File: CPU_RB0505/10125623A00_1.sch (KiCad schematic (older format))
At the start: 65 parts, among them IC3 K6R4016C1D-TI10, IC4 ST10F276, IC40 CD74HCT245M, IC41 74HCT1G04GW, IC42 74HCT1G32GW, IC43 74HCT1G32GW, IC44 NC7SZ66, Q1 8MHz, T6 2N7002

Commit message: ran renameSchSyms.py
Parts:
- C1, C3: symbol Flipped_Devices:C_Small -> Capacitor:C0603_22pF_50V_5%
- C10, C110, C116, C120, C22, C23, C25, C26, C27, C28, C29, C36, C51, C9: symbol Flipped_Devices:C_Small -> Capacitor:C0402_100nF_16V_10%
- C112, C114: symbol Flipped_Devices:C_Small -> Capacitor:C0805_1uF_16V_10%
- C14: symbol cpu-board:RES_4CB -> Capacitor:RES_4CB
- C6: symbol Flipped_Devices:C_Small -> Capacitor:C0805_330nF_16V_10%
- C7, C8: symbol Flipped_Devices:CP_Small -> Capacitor:C_1uF_35V_10%
- D10, D9: symbol Flipped_Devices:D_Schottky_A1K3 -> Diode:D_Schottky_A1K3_10022652
- D8: symbol Flipped_Devices:D_Zener_A1K3 -> Diode:D_Zener_A1K3_10022655
- Q1: symbol Device:Crystal_Small -> Crystal:Crystal_Small_10020993
- R1: symbol Flipped_Devices:R -> Resistor:R_100R_5%
- R10: symbol Flipped_Devices:R -> Resistor:R0603_1k5_5%
- R14: symbol Flipped_Devices:R -> Resistor:R0603_56k_1%
- R15: symbol Flipped_Devices:R -> Resistor:R0603_10k5_0.1%
- R3: symbol Flipped_Devices:R -> Resistor:R0603_220k_5%
- R46: symbol Flipped_Devices:R -> Resistor:R0603_22k_1%_10095983
- R60, R61: symbol Flipped_Devices:R -> Resistor:R_100k_5%
- R62: symbol Flipped_Devices:R -> Resistor:R0603_10k_5%
- R72: symbol Flipped_Devices:R -> Resistor:R_4k7_5%
- T6: symbol Flipped_Devices:Q_NMOS_GSD -> Transistor:Q_NMOS_GSD_10097274
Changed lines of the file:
@@
 $EndComp
 $Comp
-L Flipped_Devices:C_Small C?
+L Capacitor:C0402_100nF_16V_10% C?
 U 1 1 CB1F8FE5
 P 14700 2150
@@
 $EndComp
 $Comp
-L Flipped_Devices:C_Small C?
+L Capacitor:C0402_100nF_16V_10% C?
 U 1 1 A05C1986
 P 7350 9650
@@
 $EndComp
 $Comp
-L Flipped_Devices:C_Small C?
+L Capacitor:C0402_100nF_16V_10% C?
 U 1 1 93AA069D
 P 7350 9800
@@
 $EndComp
 $Comp
-L Flipped_Devices:C_Small C?
+L Capacitor:C0402_100nF_16V_10% C?
 U 1 1 5F5D481B
 P 7350 9950
@@
 $EndComp
 $Comp
-L Flipped_Devices:C_Small C?
+L Capacitor:C0402_100nF_16V_10% C?
 U 1 1 0EABB629
 P 7350 10100
@@
 $EndComp
 $Comp
-L Flipped_Devices:C_Small C?
+L Capacitor:C0402_100nF_16V_10% C?
 U 1 1 C9504634
 P 7350 10250
@@
 $EndComp
 $Comp
-L Flipped_Devices:C_Small C?
+L Capacitor:C0402_100nF_16V_10% C?
 U 1 1 AB97CB13
 P 7350 10400
@@
 $EndComp
 $Comp
-L Flipped_Devices:C_Small C?
+L Capacitor:C0402_100nF_16V_10% C?
 U 1 1 BCAFF6B0
 P 7350 10550
@@
 $EndComp
 $Comp
-L Flipped_Devices:C_Small C?
+L Capacitor:C0402_100nF_16V_10% C?
 U 1 1 284AD347
 P 7350 10700
@@
 $EndComp
 $Comp
-L Device:Crystal_Small Q?
+L Crystal:Crystal_Small_10020993 Q?
 U 1 1 F8782F37
 P 5650 1150
@@
 $EndComp
 $Comp
-L Flipped_Devices:R R?
+L Resistor:R_100R_5% R?
 U 1 1 E6C7F8B8
 P 5550 1350
@@
 $EndComp
 $Comp
-L Flipped_Devices:C_Small C?
+L Capacitor:C0805_330nF_16V_10% C?
 U 1 1 967579EA
 P 6550 1300
@@
 $EndComp
 $Comp
-L Flipped_Devices:CP_Small C?
+L Capacitor:C_1uF_35V_10% C?
 U 1 1 6D37B6AD
 P 7400 1100
@@
 $EndComp
 $Comp
-L Flipped_Devices:C_Small C?
+L Capacitor:C0402_100nF_16V_10% C?
 U 1 1 501DA122
 P 8450 1300
@@
 $EndComp
 $Comp
-L Flipped_Devices:C_Small C?
+L Capacitor:C0603_22pF_50V_5% C?
 U 1 1 7EE2FFE3
 P 5750 1050
@@
 $EndComp
 $Comp
-L Flipped_Devices:C_Small C?
+L Capacitor:C0603_22pF_50V_5% C?
 U 1 1 5ADCC44B
 P 5550 1050
@@
 $EndComp
 $Comp
-L Flipped_Devices:R R?
+L Resistor:R0603_56k_1% R?
 U 1 1 C54AB7D0
 P 2200 9550
@@
 $EndComp
 $Comp
-L Flipped_Devices:R R?
+L Resistor:R0603_10k5_0.1% R?
 U 1 1 BAB36D42
 P 2200 9850
@@
 $EndComp
 $Comp
-L Flipped_Devices:C_Small C?
+L Capacitor:C0402_100nF_16V_10% C?
 U 1 1 597E8BEF
 P 2200 10050
@@
 $EndComp
 $Comp
-L Flipped_Devices:R R?
+L Resistor:R0603_1k5_5% R?
 U 1 1 D628991E
 P 3100 5950
@@
 $EndComp
 $Comp
-L cpu-board:RES_4CB C?
+L Capacitor:RES_4CB C?
 U 1 1 8BD8962D
 P 2150 3950
@@
 $EndComp
 $Comp
-L Flipped_Devices:C_Small C?
+L Capacitor:C0402_100nF_16V_10% C?
 U 1 1 662809D9
 P 11150 1200
@@
 $EndComp
 $Comp
-L Flipped_Devices:D_Zener_A1K3 D?
+L Diode:D_Zener_A1K3_10022655 D?
 U 1 1 8A392F19
 P 12400 4250
@@
 $EndComp
 $Comp
-L Flipped_Devices:R R?
+L Resistor:R_4k7_5% R?
 U 1 1 CEF2471C
 P 12650 4050
@@
 $EndComp
 $Comp
-L Flipped_Devices:R R?
+L Resistor:R_100k_5% R?
 U 1 1 CCBE402C
 P 12050 7250
@@
 $EndComp
 $Comp
-L Flipped_Devices:C_Small C?
+L Capacitor:C0805_1uF_16V_10% C?
 U 1 1 9A495DAC
 P 12200 7250
@@
 $EndComp
 $Comp
-L Flipped_Devices:D_Schottky_A1K3 D?
+L Diode:D_Schottky_A1K3_10022652 D?
 U 1 1 59396773
 P 13950 7700
@@
 $EndComp
 $Comp
-L Flipped_Devices:R R?
+L Resistor:R0603_10k_5% R?
 U 1 1 F7CB6097
 P 4800 10950
@@
 $EndComp
 $Comp
-L Flipped_Devices:C_Small C?
+L Capacitor:C0402_100nF_16V_10% C?
 U 1 1 7614D321
 P 4800 10550
@@
 $EndComp
 $Comp
-L Flipped_Devices:C_Small C?
+L Capacitor:C0402_100nF_16V_10% C?
 U 1 1 150190AD
 P 10200 3250
@@
 	7950 1500 7950 1100
 $Comp
-L Flipped_Devices:CP_Small C?
+L Capacitor:C_1uF_35V_10% C?
 U 1 1 6F4029DE
 P 8250 1300
@@
 	12200 7700 12050 7700
 $Comp
-L Flipped_Devices:Q_NMOS_GSD T?
+L Transistor:Q_NMOS_GSD_10097274 T?
 U 1 1 78F4DB2D
 P 11850 6700
@@
 $EndComp
 $Comp
-L Flipped_Devices:R R?
+L Resistor:R0603_22k_1%_10095983 R?
 U 1 1 CBBF32AF
 P 12450 6700
@@
 Connection ~ 12050 6700
 $Comp
-L Flipped_Devices:D_Schottky_A1K3 D?
+L Diode:D_Schottky_A1K3_10022652 D?
 U 1 1 13A4EF58
 P 12450 6400
@@
 	14900 6850 14900 6800
 $Comp
-L Flipped_Devices:C_Small C?
+L Capacitor:C0805_1uF_16V_10% C?
 U 1 1 C17297D4
 P 14150 7300
@@
 Connection ~ 13650 7300
 $Comp
-L Flipped_Devices:R R?
+L Resistor:R_100k_5% R?
 U 1 1 CC254D70
 P 13800 7700
@@
 	5950 1550 5950 1600
 $Comp
-L Flipped_Devices:R R?
+L Resistor:R0603_220k_5% R?
 U 1 1 E7C109B0
 P 7150 1200

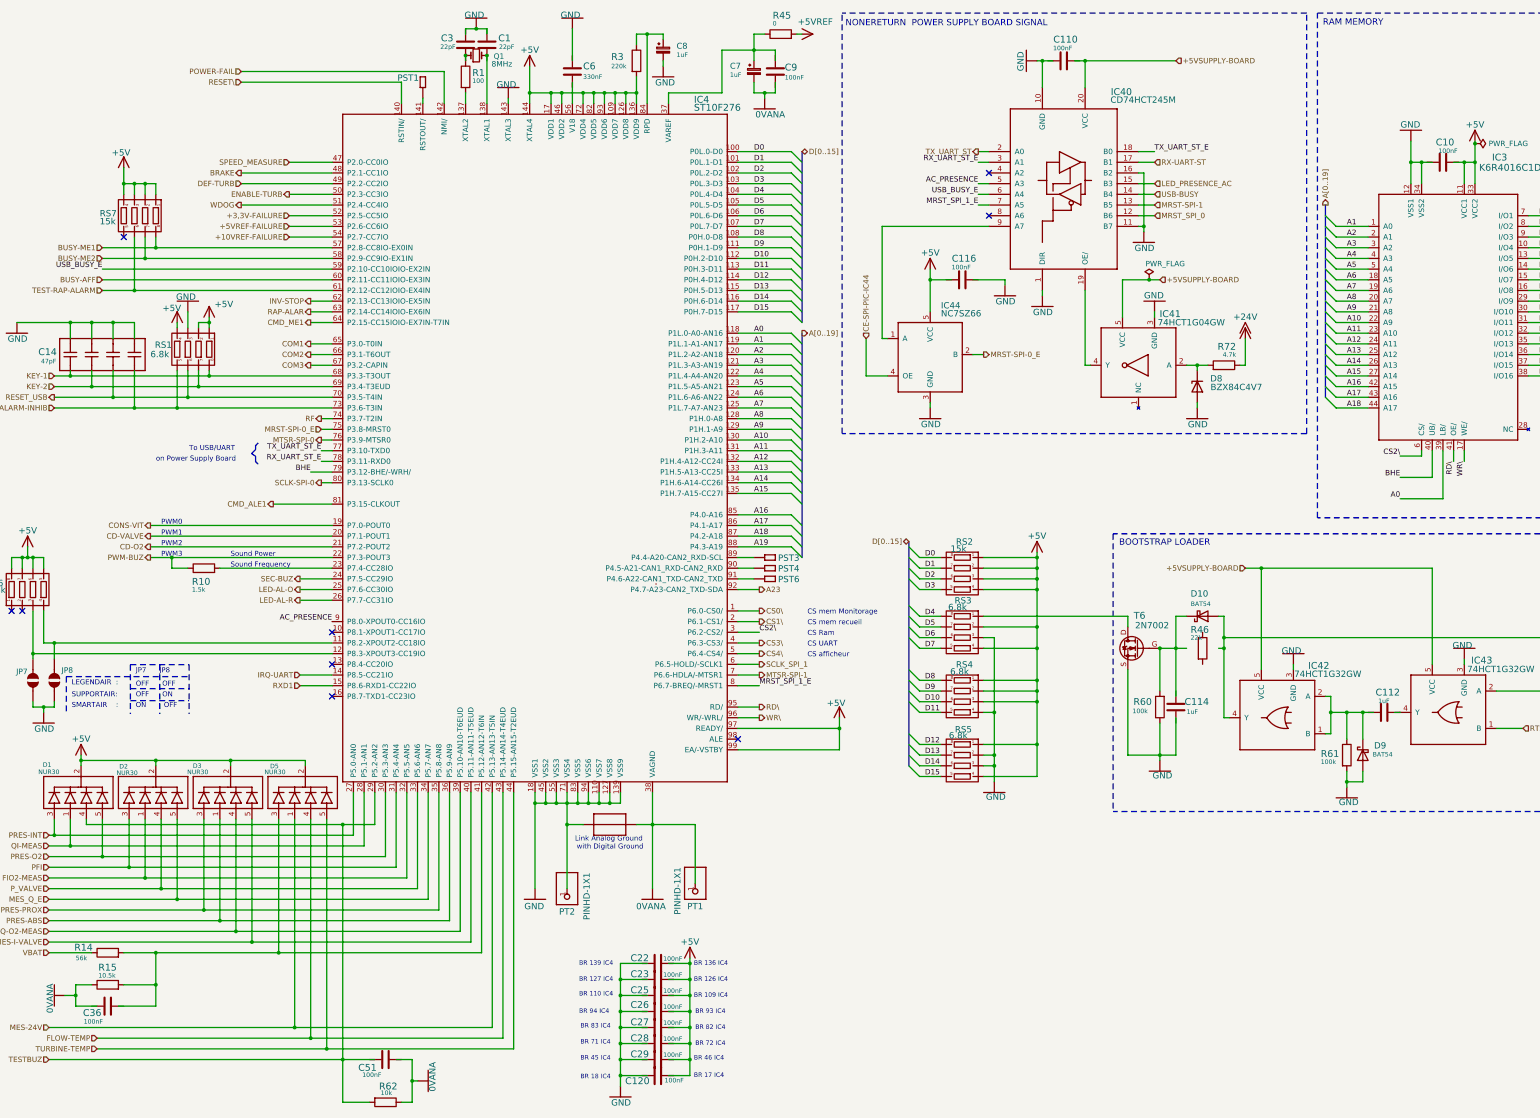
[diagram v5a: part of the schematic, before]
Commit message: CPU board passed ERC and matches Update PCB report
Schematic needs cleanup!
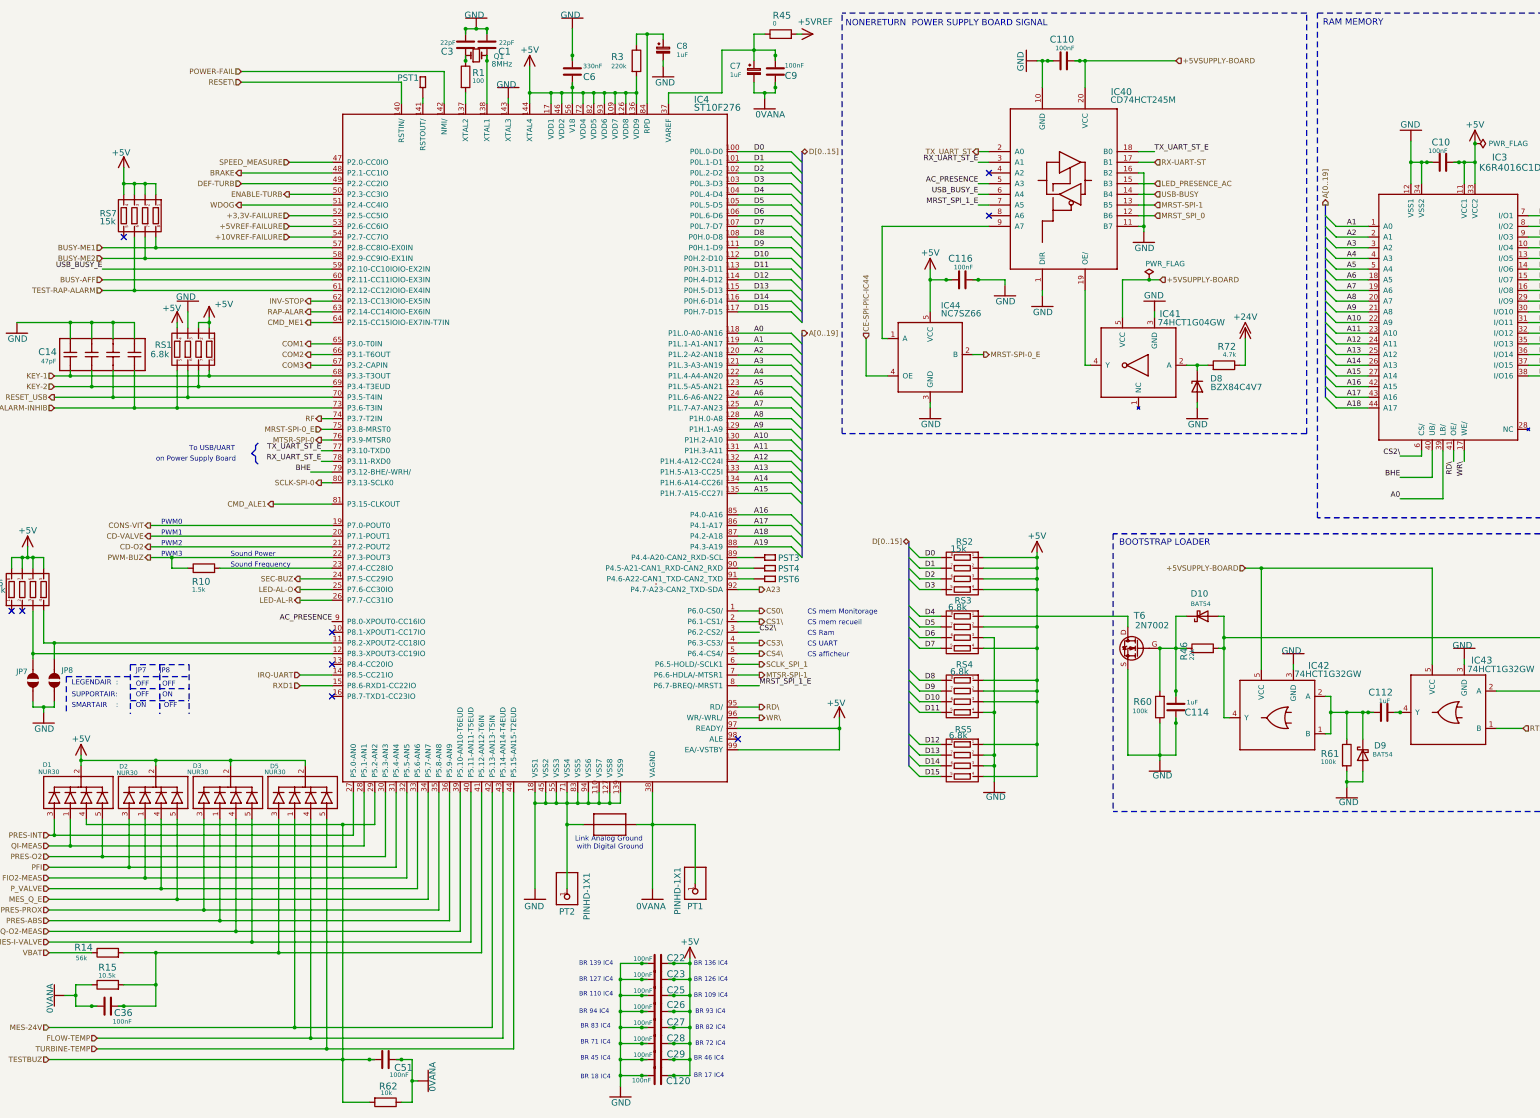
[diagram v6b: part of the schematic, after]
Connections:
- wire segments 558 -> 592
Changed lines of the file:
@@
 F 17 "MONOLITHIC CERAMIC CAPACITOR" H 14700 2150 50  0001 C CNN "Manufacturer_Desc4"
 	1    14700 2150
-	0    -1   -1   0
+	0    1    -1   0
 $EndComp
 $Comp
@@
 F 17 "MONOLITHIC CERAMIC CAPACITOR" H 7350 9650 50  0001 C CNN "Manufacturer_Desc4"
 	1    7350 9650
-	0    1    1    0
+	0    -1   1    0
 $EndComp
 $Comp
@@
 F 17 "MONOLITHIC CERAMIC CAPACITOR" H 7350 9800 50  0001 C CNN "Manufacturer_Desc4"
 	1    7350 9800
-	0    1    1    0
+	0    -1   1    0
 $EndComp
 $Comp
@@
 F 17 "MONOLITHIC CERAMIC CAPACITOR" H 7350 9950 50  0001 C CNN "Manufacturer_Desc4"
 	1    7350 9950
-	0    1    1    0
+	0    -1   1    0
 $EndComp
 $Comp
@@
 F 17 "MONOLITHIC CERAMIC CAPACITOR" H 7350 10100 50  0001 C CNN "Manufacturer_Desc4"
 	1    7350 10100
-	0    1    1    0
+	0    -1   1    0
 $EndComp
 $Comp
@@
 F 17 "MONOLITHIC CERAMIC CAPACITOR" H 7350 10250 50  0001 C CNN "Manufacturer_Desc4"
 	1    7350 10250
-	0    1    1    0
+	0    -1   1    0
 $EndComp
 $Comp
@@
 F 17 "MONOLITHIC CERAMIC CAPACITOR" H 7350 10400 50  0001 C CNN "Manufacturer_Desc4"
 	1    7350 10400
-	0    1    1    0
+	0    -1   1    0
 $EndComp
 $Comp
@@
 F 17 "MONOLITHIC CERAMIC CAPACITOR" H 7350 10550 50  0001 C CNN "Manufacturer_Desc4"
 	1    7350 10550
-	0    1    1    0
+	0    -1   1    0
 $EndComp
 $Comp
@@
 F 3 "" H 7350 10700 50  0001 C CNN
 	1    7350 10700
-	0    1    1    0
+	0    -1   1    0
 $EndComp
 $Comp
@@
 F 20 "CAPACITOR, CERAMIC, MULTILAYER, 16 V, X7R, 0.33 UF, SURFACE MOUNT, 0805" H 6550 1300 50  0001 C CNN "Manufacturer_Desc5"
 	1    6550 1300
-	1    0    0    -1
+	1    0    0    1
 $EndComp
 $Comp
@@
 F 17 "MONOLITHIC CERAMIC CAPACITOR" H 8450 1300 50  0001 C CNN "Manufacturer_Desc4"
 	1    8450 1300
-	1    0    0    -1
+	1    0    0    1
 $EndComp
 $Comp
@@
 F 14 "CAPACITOR, CERAMIC, MULTILAYER, 50 V, C0G, 0.000022 UF, SURFACE MOUNT, 0603" H 5750 1050 50  0001 C CNN "Manufacturer_Desc3"
 	1    5750 1050
-	1    0    0    -1
+	1    0    0    1
 $EndComp
 $Comp
@@
 F 14 "CAPACITOR, CERAMIC, MULTILAYER, 50 V, C0G, 0.000022 UF, SURFACE MOUNT, 0603" H 5550 1050 50  0001 C CNN "Manufacturer_Desc3"
 	1    5550 1050
-	1    0    0    -1
+	1    0    0    1
 $EndComp
 $Comp
@@
 F 17 "MONOLITHIC CERAMIC CAPACITOR" H 2200 10050 50  0001 C CNN "Manufacturer_Desc4"
 	1    2200 10050
-	0    -1   -1   0
+	0    1    -1   0
 $EndComp
 $Comp
@@
 F 3 "" H 11150 1200 50  0001 C CNN
 	1    11150 1200
-	0    -1   -1   0
+	0    1    -1   0
 $EndComp
 $Comp
@@
 F 17 "MONOLITHIC CERAMIC CAPACITOR" H 12200 7250 50  0001 C CNN "Manufacturer_Desc4"
 	1    12200 7250
-	1    0    0    -1
+	1    0    0    1
 $EndComp
 $Comp
@@
 F 17 "MONOLITHIC CERAMIC CAPACITOR" H 4800 10550 50  0001 C CNN "Manufacturer_Desc4"
 	1    4800 10550
-	0    1    1    0
+	0    -1   1    0
 $EndComp
 $Comp
@@
 F 3 "" H 10200 3250 50  0001 C CNN
 	1    10200 3250
-	0    -1   -1   0
+	0    1    -1   0
 $EndComp
 $Comp
@@
 	8250 1400 8250 1500
 Wire Wire Line
-	8450 1500 8450 1400
-Wire Wire Line
 	8350 1500 8350 1550
 Wire Wire Line
@@
 	7950 1100 8250 1100
 Wire Wire Line
-	8450 1100 8450 1200
-Wire Wire Line
 	8250 1200 8250 1100
 Connection ~ 8250 1100
@@
 	7050 1500 7150 1500
 Wire Wire Line
-	6550 1200 6550 900
+	6550 1200 6550 1150
 Wire Wire Line
 	6150 1600 6150 1500
 Wire Wire Line
-	6550 1400 6550 1600
+	6550 1400 6550 1450
 Wire Wire Line
 	6650 1500 6450 1500
@@
 	6150 1500 6150 1250
 Wire Wire Line
-	5750 1600 5750 1150
-Connection ~ 5750 1150
+	5750 1600 5750 1200
 Wire Wire Line
 	5750 950  5750 900
@@
 Connection ~ 14900 2150
 Wire Wire Line
-	14900 2150 14800 2150
+	14900 2150 14850 2150
 Wire Wire Line
-	14600 2150 14500 2150
+	14600 2150 14550 2150
 Wire Wire Line
 	14400 2150 14400 1950
@@
 	2650 9550 2650 9850
 Wire Wire Line
-	2650 10050 2300 10050
+	2650 10050 2350 10050
 Connection ~ 2650 9850
 Wire Wire Line
@@
 	1900 9950 1900 10050
 Wire Wire Line
-	1900 10050 2100 10050
+	1900 10050 2050 10050
 Connection ~ 1900 9950
 Wire Wire Line
@@
 Connection ~ 4400 10550
 Wire Wire Line
-	4400 10550 4700 10550
+	4400 10550 4650 10550
 Wire Wire Line
-	4900 10550 5050 10550
+	4900 10550 4950 10550
 Wire Wire Line
 	5050 10550 5050 10750
@@
 	4400 10550 4400 10950
 Wire Wire Line
-	11050 1200 10950 1200
+	11050 1200 11000 1200
 Wire Wire Line
 	10950 1450 10950 1200
@@
 	10950 1200 10900 1200
 Wire Wire Line
-	11250 1200 11350 1200
+	11250 1200 11300 1200
 Wire Wire Line
 	11350 1450 11350 1200
@@
 	7000 10800 7000 10700
 Wire Wire Line
-	7000 9650 7250 9650
+	7000 9650 7200 9650
 Wire Wire Line
-	7250 9800 7000 9800
+	7250 9800 7200 9800
 Connection ~ 7000 9800
 Wire Wire Line
@@
 	7650 9600 7650 9650
 Wire Wire Line
-	7650 10700 7450 10700
+	7650 10700 7500 10700
 Wire Wire Line
-	7250 10700 7000 10700
+	7250 10700 7200 10700
 Connection ~ 7000 10700
 Wire Wire Line
 	7000 10700 7000 10550
 Wire Wire Line
-	7250 10550 7000 10550
+	7250 10550 7200 10550
 Connection ~ 7000 10550
 Wire Wire Line
 	7000 10550 7000 10400
 Wire Wire Line
-	7250 10400 7000 10400
+	7250 10400 7200 10400
 Connection ~ 7000 10400
 Wire Wire Line
 	7000 10400 7000 10250
 Wire Wire Line
-	7250 10250 7000 10250
+	7250 10250 7200 10250
 Connection ~ 7000 10250
 Wire Wire Line
 	7000 10250 7000 10100
 Wire Wire Line
-	7250 10100 7000 10100
+	7250 10100 7200 10100
 Connection ~ 7000 10100
 Wire Wire Line
 	7000 10100 7000 9950
 Wire Wire Line
-	7250 9950 7000 9950
+	7250 9950 7200 9950
 Connection ~ 7000 9950
 Wire Wire Line
 	7000 9950 7000 9800
 Wire Wire Line
-	7450 9950 7650 9950
+	7450 9950 7500 9950
 Connection ~ 7650 9950
 Wire Wire Line
 	7650 9950 7650 10100
 Wire Wire Line
-	7450 10100 7650 10100
+	7450 10100 7500 10100
 Connection ~ 7650 10100
 Wire Wire Line
 	7650 10100 7650 10250
 Wire Wire Line
-	7450 10250 7650 10250
+	7450 10250 7500 10250
 Connection ~ 7650 10250
 Wire Wire Line
 	7650 10250 7650 10400
 Wire Wire Line
-	7450 10400 7650 10400
+	7450 10400 7500 10400
 Connection ~ 7650 10400
 Wire Wire Line
 	7650 10400 7650 10550
 Wire Wire Line
-	7650 10550 7450 10550
+	7650 10550 7500 10550
 Connection ~ 7650 10550
 Wire Wire Line
 	7650 10550 7650 10700
 Wire Wire Line
-	7450 9800 7650 9800
+	7450 9800 7500 9800
 Connection ~ 7650 9800
 Wire Wire Line
 	7650 9800 7650 9950
 Wire Wire Line
-	7650 9650 7450 9650
+	7650 9650 7500 9650
 Connection ~ 7650 9650
 Wire Wire Line
@@
 Connection ~ 12050 7700
 Wire Wire Line
-	12200 7350 12200 7700
+	12200 7350 12200 7400
 Wire Wire Line
 	12200 7700 12050 7700
@@
 F 14 "RESISTOR, METAL GLAZE/THICK FILM, 0.1 W, 1 %, 100 PPM, 22000 OHM, SURFACE MOUNT, 0603" H 12450 6700 50  0001 C CNN "Manufacturer_Desc3"
 	1    12450 6700
-	1    0    0    -1
+	0    -1   -1   0
 $EndComp
 Wire Wire Line
-	12200 7150 12200 6700
+	12200 7150 12200 7100
 Wire Wire Line
 	12200 6700 12050 6700
@@
 F 17 "MONOLITHIC CERAMIC CAPACITOR" H 14150 7300 50  0001 C CNN "Manufacturer_Desc4"
 	1    14150 7300
-	0    1    1    0
+	0    -1   1    0
 $EndComp
 $Comp
@@
 	14250 7300 14300 7300
 Wire Wire Line
-	14050 7300 13950 7300
+	14050 7300 14000 7300
 Connection ~ 13950 7300
 NoConn ~ 10450 2250
@@
 	9900 3150 9900 3250
 Wire Wire Line
-	10100 3250 9900 3250
+	10100 3250 10050 3250
 Connection ~ 9900 3250
 Wire Wire Line
 	9900 3250 9900 3550
 Wire Wire Line
-	10300 3250 10600 3250
+	10300 3250 10350 3250
 Wire Wire Line
 	10600 3250 10600 3300
@@
 Wire Wire Line
 	5550 1200 5550 1150
-Connection ~ 5550 1150
 Wire Wire Line
 	5550 1500 5550 1600
@@
 Wire Wire Line
 	13950 7850 13950 7950
+Connection ~ 2050 10050
+Wire Wire Line
+	2050 10050 2100 10050
+Connection ~ 2350 10050
+Wire Wire Line
+	2350 10050 2300 10050
+Connection ~ 4950 10550
+Wire Wire Line
+	4950 10550 5050 10550
+Connection ~ 4650 10550
+Wire Wire Line
+	4650 10550 4700 10550
+Connection ~ 7200 9650
+Wire Wire Line
+	7200 9650 7250 9650
+Connection ~ 7200 9800
+Wire Wire Line
+	7200 9800 7000 9800
+Connection ~ 7200 9950
+Wire Wire Line
+	7200 9950 7000 9950
+Connection ~ 7200 10100
+Wire Wire Line
+	7200 10100 7000 10100
+Connection ~ 7200 10250
+Wire Wire Line
+	7200 10250 7000 10250
+Connection ~ 7200 10400
+Wire Wire Line
+	7200 10400 7000 10400
+Connection ~ 7200 10550
+Wire Wire Line
+	7200 10550 7000 10550
+Connection ~ 7200 10700
+Wire Wire Line
+	7200 10700 7000 10700
+Connection ~ 7500 9650
+Wire Wire Line
+	7500 9650 7450 9650
+Connection ~ 7500 9800
+Wire Wire Line
+	7500 9800 7650 9800
+Connection ~ 7500 9950
+Wire Wire Line
+	7500 9950 7650 9950
+Connection ~ 7500 10100
+Wire Wire Line
+	7500 10100 7650 10100
+Connection ~ 7500 10250
+Wire Wire Line
+	7500 10250 7650 10250
+Connection ~ 7500 10400
+Wire Wire Line
+	7500 10400 7650 10400
+Connection ~ 7500 10550
+Wire Wire Line
+	7500 10550 7450 10550
+Connection ~ 7500 10700
+Wire Wire Line
+	7500 10700 7450 10700
+Connection ~ 14300 7300
+Connection ~ 14000 7300
+Wire Wire Line
+	14000 7300 13950 7300
+Connection ~ 12200 7100
+Wire Wire Line
+	12200 7100 12200 6700
+Connection ~ 12200 7400
+Wire Wire Line
+	12200 7400 12200 7700
+Connection ~ 14550 2150
+Wire Wire Line
+	14550 2150 14500 2150
+Connection ~ 14850 2150
+Wire Wire Line
+	14850 2150 14800 2150
+Connection ~ 11000 1200
+Wire Wire Line
+	11000 1200 10950 1200
+Connection ~ 11300 1200
+Wire Wire Line
+	11300 1200 11350 1200
+Connection ~ 10050 3250
+Wire Wire Line
+	10050 3250 9900 3250
+Connection ~ 10350 3250
+Wire Wire Line
+	10350 3250 10600 3250
+Connection ~ 6550 1150
+Wire Wire Line
+	6550 1150 6550 900
+Connection ~ 6550 1450
+Wire Wire Line
+	6550 1450 6550 1600
+Connection ~ 5750 900
+Connection ~ 5750 1200
+Wire Wire Line
+	5750 1200 5750 1150
+Connection ~ 5550 900
+Connection ~ 5550 1200
+Wire Wire Line
+	8450 1400 8450 1450
+Wire Wire Line
+	8450 1100 8450 1150
+Connection ~ 8450 1150
+Wire Wire Line
+	8450 1150 8450 1200
+Connection ~ 8450 1450
+Wire Wire Line
+	8450 1450 8450 1500
 Wire Bus Line
 	15950 2650 15950 4250
